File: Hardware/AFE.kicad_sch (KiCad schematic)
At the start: 32 parts, among them U2 REF3220AMDBVREP

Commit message: fix: #145, fix: #159
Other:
- company: (none) -> RG
- title: (none) -> TIA & Differential ADC Driver
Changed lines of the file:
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@@
 	(generator_version "10.0")
 	(paper "A4")
+	(title_block
+		(title "TIA & Differential ADC Driver")
+		(date "2026-04-06")
+		(rev "1.0")
+		(company "RG")
+	)
 	(text "Filtering capacitors for AD8139,\nshould be placed close to the chip."
 		(exclude_from_sim no)
@@
 	(text "All capcititors (except for voltage filtering) are  C0G / NP0.\nAll resistors are 1% or better."
 		(exclude_from_sim no)
-		(at 156.21 133.35 0)
+		(at 175.26 86.36 0)
 		(effects
 			(font
@@
 			(table_cell "Label"
 				(exclude_from_sim no)
-				(at 154.94 137.16 0)
+				(at 173.99 90.17 0)
 				(size 15.24 3.81)
 				(margins 0.9525 0.9525 0.9525 0.9525)
@@
 			(table_cell "Description"
 				(exclude_from_sim no)
-				(at 170.18 137.16 0)
+				(at 189.23 90.17 0)
 				(size 54.61 3.81)
 				(margins 0.9525 0.9525 0.9525 0.9525)
@@
 			(table_cell "VCC_SIPM"
 				(exclude_from_sim no)
-				(at 154.94 140.97 0)
+				(at 173.99 93.98 0)
 				(size 15.24 3.81)
 				(margins 0.9525 0.9525 0.9525 0.9525)
@@
 			(table_cell "28.89V-29.22V (+322.5mV over 15degC) SiPM bias"
 				(exclude_from_sim no)
-				(at 170.18 140.97 0)
+				(at 189.23 93.98 0)
 				(size 54.61 3.81)
 				(margins 0.9525 0.9525 0.9525 0.9525)
@@
 			(table_cell "VCC_5V"
 				(exclude_from_sim no)
-				(at 154.94 144.78 0)
+				(at 173.99 97.79 0)
 				(size 15.24 3.81)
 				(margins 0.9525 0.9525 0.9525 0.9525)
@@
 			(table_cell "Differential ADC Driver and its reference voltage"
 				(exclude_from_sim no)
-				(at 170.18 144.78 0)
+				(at 189.23 97.79 0)
 				(size 54.61 3.81)
 				(margins 0.9525 0.9525 0.9525 0.9525)
@@
 			(table_cell "VCC_5V"
 				(exclude_from_sim no)
-				(at 154.94 148.59 0)
+				(at 173.99 101.6 0)
 				(size 15.24 3.81)
 				(margins 0.9525 0.9525 0.9525 0.9525)
@@
 			(table_cell "Differential ADC Driver"
 				(exclude_from_sim no)
-				(at 170.18 148.59 0)
+				(at 189.23 101.6 0)
 				(size 54.61 3.81)
 				(margins 0.9525 0.9525 0.9525 0.9525)
@@
 			(table_cell "VCC_2V5"
 				(exclude_from_sim no)
-				(at 154.94 152.4 0)
+				(at 173.99 105.41 0)
 				(size 15.24 3.81)
 				(margins 0.9525 0.9525 0.9525 0.9525)
@@
 			(table_cell "TIA"
 				(exclude_from_sim no)
-				(at 170.18 152.4 0)
+				(at 189.23 105.41 0)
 				(size 54.61 3.81)
 				(margins 0.9525 0.9525 0.9525 0.9525)
@@
 			(table_cell "VEE_2V5"
 				(exclude_from_sim no)
-				(at 154.94 156.21 0)
+				(at 173.99 109.22 0)
 				(size 15.24 3.81)
 				(margins 0.9525 0.9525 0.9525 0.9525)
@@
 			(table_cell "TIA"
 				(exclude_from_sim no)
-				(at 170.18 156.21 0)
+				(at 189.23 109.22 0)
 				(size 54.61 3.81)
 				(margins 0.9525 0.9525 0.9525 0.9525)
@@
 	)
 	(hierarchical_label "{SIPM_ADC}"
-		(shape input)
+		(shape output)
 		(at 154.94 50.8 0)
 		(effects

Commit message: fix: #160, fix: #163, fix: #164
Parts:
- removed C12: 470n, Capacitor_SMD:C_0805_2012Metric, symbol Device:C
- removed TP3: TestPoint, TestPoint:TestPoint_Pad_D1.5mm, symbol Connector:TestPoint
- removed U2: REF3220AMDBVREP, Package_TO_SOT_SMD:SOT-23-6, symbol Reference_Voltage:REF3220AMDBVREP
- U3: value (none) -> LTC6268IS6
- U4: value (none) -> AD8139
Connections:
- net ADC_REF renamed +2V048_VREF
- net NEG renamed AFE_OUT_N
- net POS renamed AFE_OUT_P
- net VCC_2V5 renamed +2V5_AFE
- net VCC_5V renamed +5V0_AFE
- net VEE_2V5 renamed -2V5_AFE
- net VEE_5V renamed -5V0_AFE
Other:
- note removed: "R13, C16 are precision elements."
- moved on the sheet: C13, C14, C15, C16, C17, C18, C20, C21, C22, C24, D1, R10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

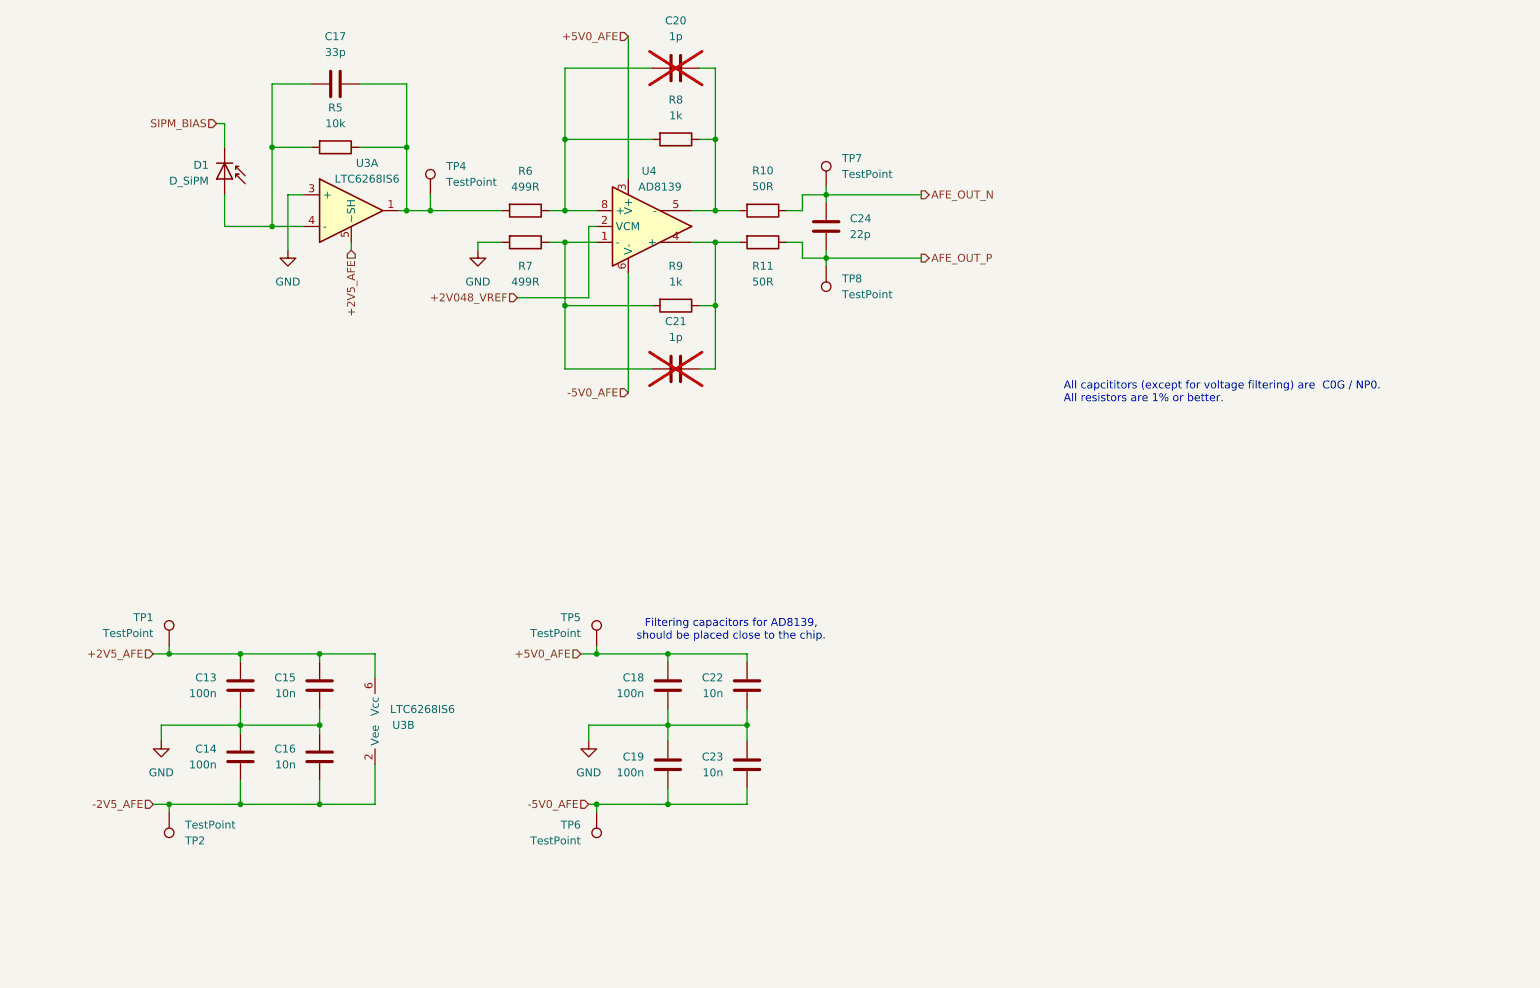
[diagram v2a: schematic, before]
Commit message: fix: #134
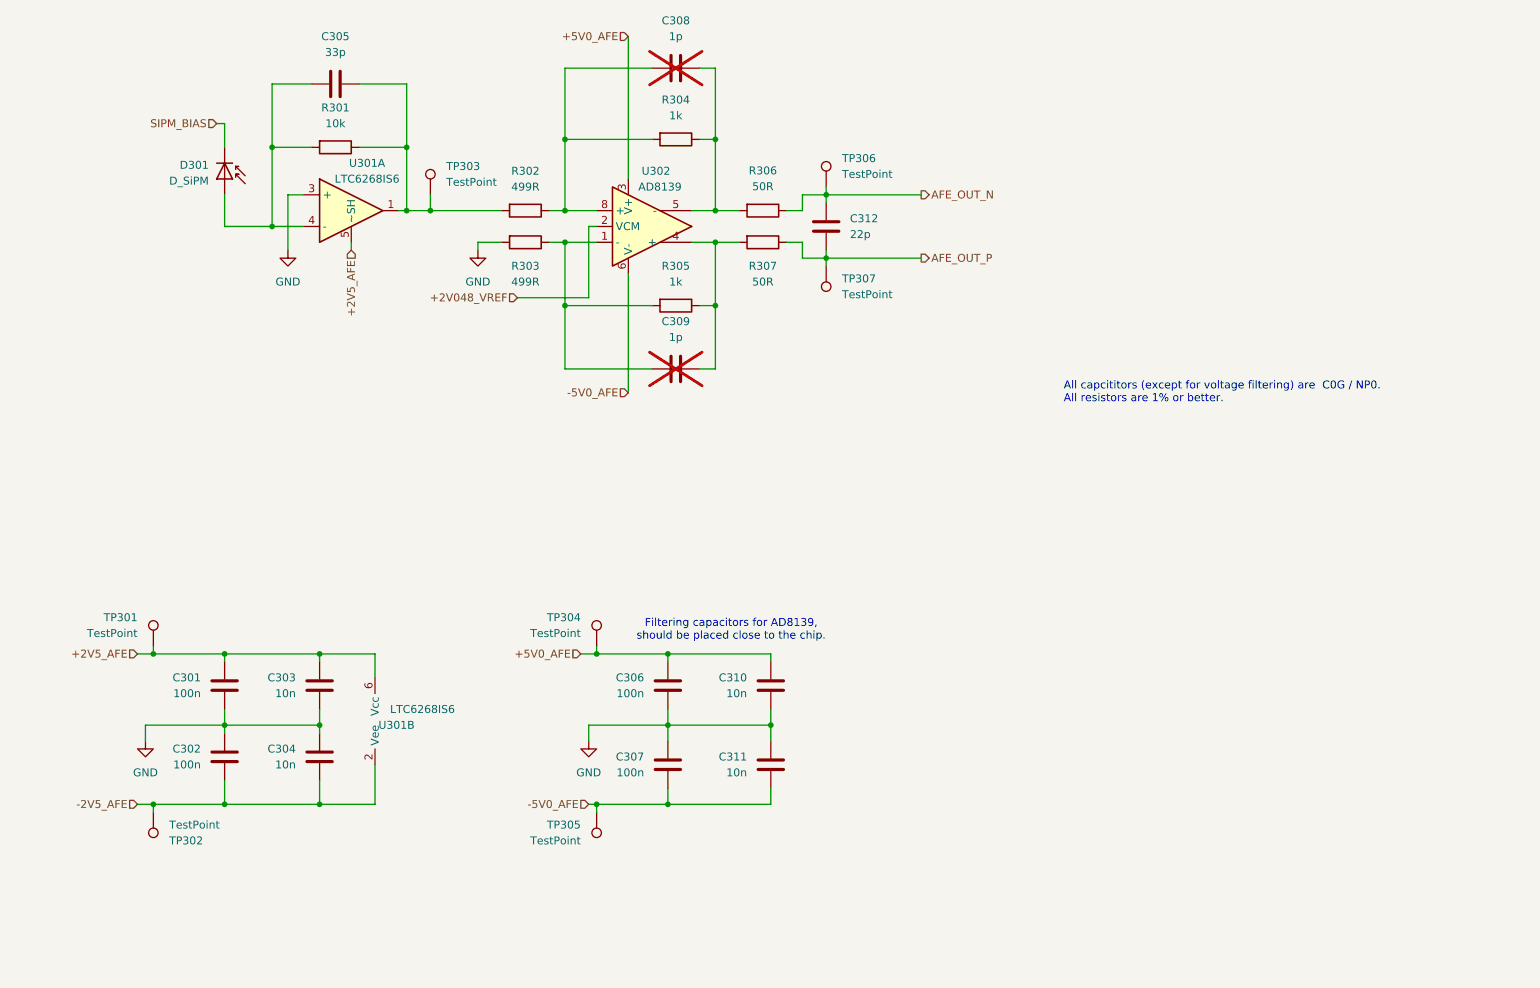
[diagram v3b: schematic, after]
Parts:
- renumbered C13 to C301, C14 to C302, C15 to C303, C16 to C304, C17 to C305, C18 to C306, C19 to C307, C20 to C308, C21 to C309, C22 to C310, C23 to C311, C24 to C312, D1 to D301, R5 to R301, R6 to R302, R7 to R303, R8 to R304, R9 to R305, R10 to R306, R11 to R307, TP1 to TP301, TP2 to TP302, TP4 to TP303, TP5 to TP304, TP6 to TP305, TP7 to TP306, TP8 to TP307, U3 to U301, U4 to U302
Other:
- moved on the sheet: C301, C302, C310, C311, TP301, TP302

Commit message: fix: #170, fix: #144, fix: #132
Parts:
- removed C305: 33p, Capacitor_SMD:C_0805_2012Metric, symbol Device:C
- removed C306, C307: 100n, Capacitor_SMD:C_0805_2012Metric, symbol Device:C
- removed C308, C309: 1p, Capacitor_SMD:C_0805_2012Metric, symbol Device:C
- removed C310, C311: 10n, Capacitor_SMD:C_0805_2012Metric, symbol Device:C
- removed C312: 22p, Capacitor_SMD:C_0805_2012Metric, symbol Device:C
- removed D301: D_SiPM, symbol Device:D_SiPM
- removed R301: 10k, Resistor_SMD:R_0805_2012Metric, symbol Device:R
- removed R302, R303: 499R, Resistor_SMD:R_0805_2012Metric, symbol Device:R
- removed R304, R305: 1k, Resistor_SMD:R_0805_2012Metric, symbol Device:R
- removed R306, R307: 50R, Resistor_SMD:R_0805_2012Metric, symbol Device:R
- removed TP301, TP302, TP303, TP304, TP305, TP306, TP307: TestPoint, TestPoint:TestPoint_Pad_D1.5mm, symbol Connector:TestPoint
- removed U301: LTC6268IS6, Package_TO_SOT_SMD:TSOT-23-6_HandSoldering, symbol DataAcquisitionUnit:LTC6268IS6_TSOT-23
- removed U302: AD8139, Package_SO:SOIC-8_5.3x5.3mm_P1.27mm, symbol DataAcquisitionUnit:AD8139
- added J301: RFShield_TwoPieces, GammaSpectrometer:BUD_CU-470_Shield, symbol Device:RFShield_TwoPieces
- added U301: ISL21010C, Package_TO_SOT_SMD:SOT-23, symbol GammaSpectrometer:ISL21010C
- C301: value 100n -> 1u
- C303: value 10n -> 1u
- C304: value 10n -> 100n
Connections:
- net -2V5_AFE is gone; now on net GND: C302.2, C304.2
- net GND: now also J301.1 (Shield), U301.3 (GND); no longer C302.1, C304.1
- net +2V5_AFE renamed +3V3_A
- net +3V3_A: now also C302.1, U301.1 (VIN); no longer C303.1
- new net AFEChannel1/1V5_REF: C303.1, C304.1, U301.2 (VOUT)
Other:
- added sheet AFEChannel1 (AFEChannel1.kicad_sch)
- added sheet AFEChannel2 (AFEChannel2.kicad_sch)
- note removed: "All capcititors (except for voltage filtering) are C0G / NP0. All resistors are 1% or better."
- note removed: "Filtering capacitors for AD8139, should be placed close to the chip."
